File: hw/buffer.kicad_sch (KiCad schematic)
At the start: 27 parts, among them K2 G6S-2, U14 AQY225R2S, U18 TS5A63157DBV, U19 OPA859xDSG, U20 AD8370

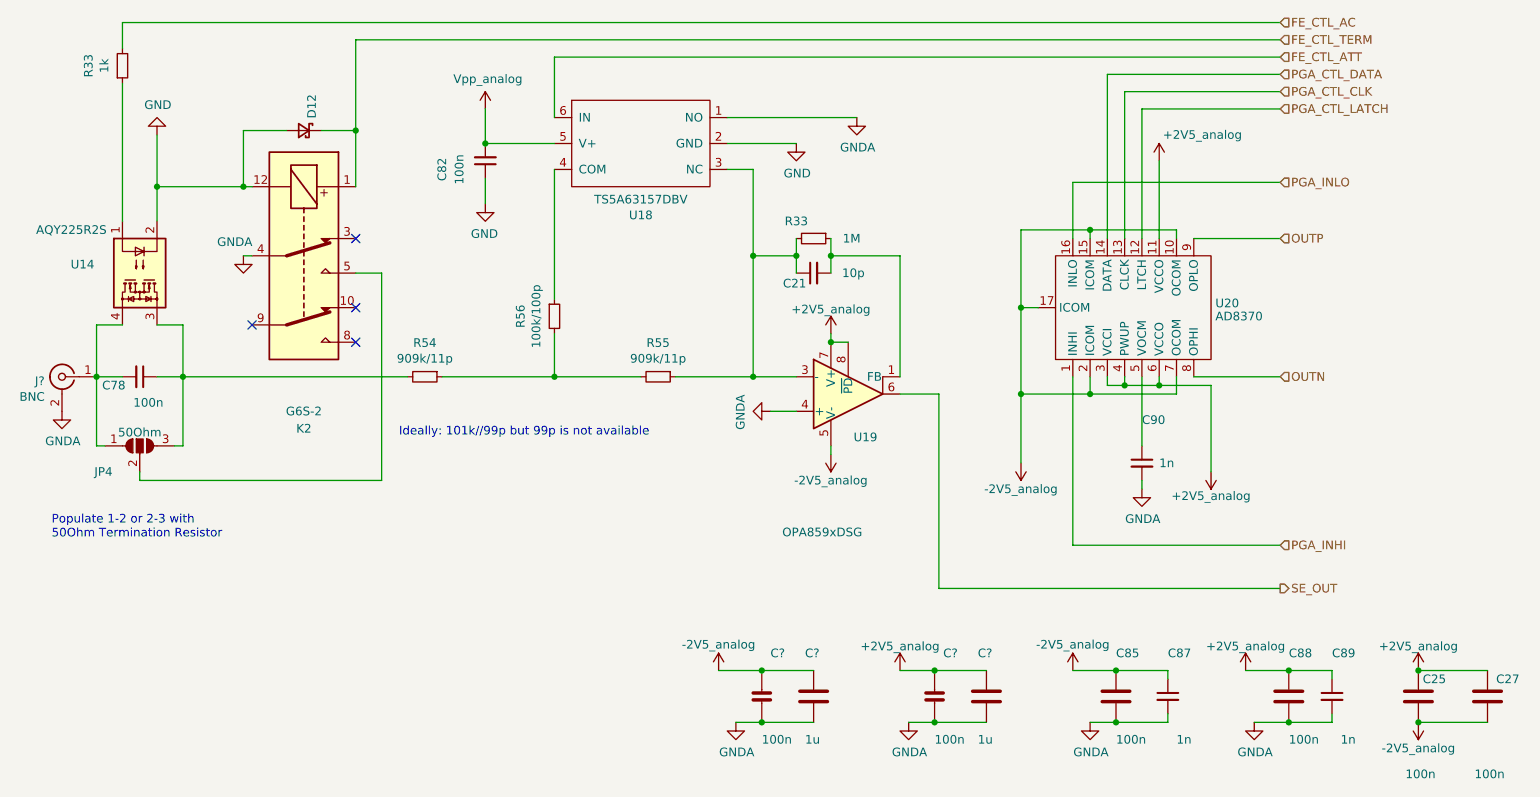
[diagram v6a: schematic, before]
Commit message: Added trion top-sheet as sub-sheet to usbadc project
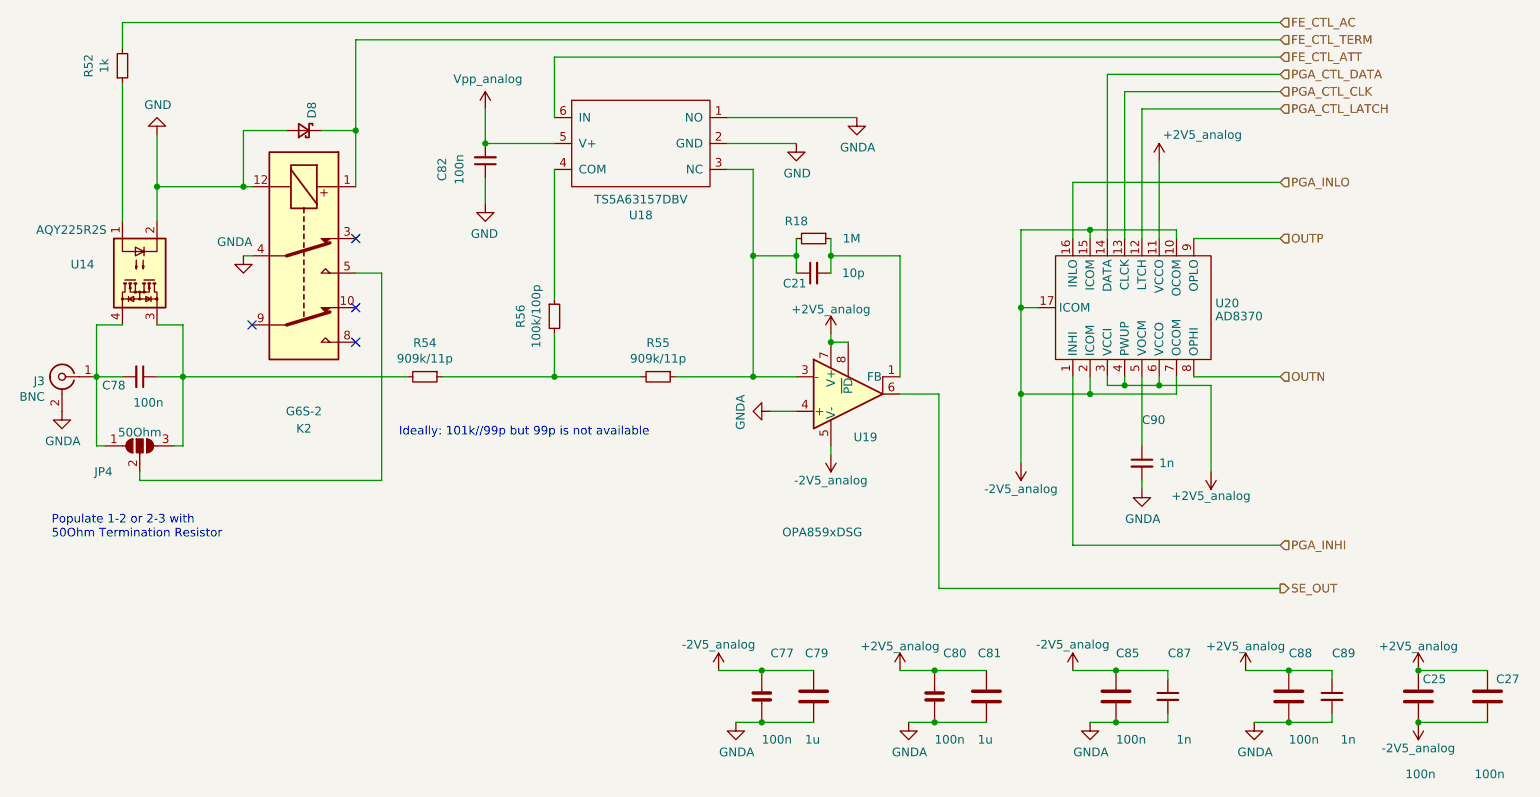
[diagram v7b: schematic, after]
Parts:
- gave numbers to parts that had none: 5
- renumbered D12 to D8, R33 to R18, R33 to R52
